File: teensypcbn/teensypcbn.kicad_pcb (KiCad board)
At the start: 2 copper layers, 4 parts, among them J1 CONN_26X2, J2 CONN_26X2, J3 629104190121, U1 Teensy4.1

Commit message: schema
schema voledig klaar
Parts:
- added BT1: Battery, Connector_JST:JST_PH_S2B-PH-SM4-TB_1x02-1MP_P2.00mm_Horizontal, F.Cu at (188.5, 20.3)
- added C1: 0.1, Capacitor_SMD:C_0603_1608Metric_Pad0.99x1.00mm_HandSolder, F.Cu at (171.6, 27.1)
- added C2: 0.1, Capacitor_SMD:C_0603_1608Metric_Pad0.99x1.00mm_HandSolder, F.Cu at (176.0, 27.2)
- added C3: 0.1, Capacitor_SMD:C_0603_1608Metric_Pad0.99x1.00mm_HandSolder, F.Cu at (195.8, 15.9)
- added C4: 0.1, Capacitor_SMD:C_0603_1608Metric_Pad0.99x1.00mm_HandSolder, F.Cu at (180.3, 27.1)
- added C5: 1000pF, Capacitor_SMD:C_0603_1608Metric_Pad0.99x1.00mm_HandSolder, F.Cu at (195.8, 18.5)
- added C6: 1000pF, Capacitor_SMD:C_0603_1608Metric_Pad0.99x1.00mm_HandSolder, F.Cu at (195.8, 21.0)
- added J4: SS-7188S-A-NF, SamacSys_Parts:SS-7188S-A-NF, F.Cu at (192.0, 49.3)
- added R1: R_US, Resistor_SMD:R_0603_1608Metric, F.Cu at (195.6, 23.6)
- added R2: R_US, Resistor_SMD:R_0603_1608Metric, F.Cu at (195.6, 26.1)
- added R3: R_US, Resistor_SMD:R_0603_1608Metric, F.Cu at (184.5, 28.7)
- added R4: R_US, Resistor_SMD:R_0603_1608Metric, F.Cu at (188.4, 27.2)
- added T1: HX1198FNLT, SamacSys_Parts:HX1198FNLT, B.Cu at (191.8, 78.5)
- moved J3 15.2 mm to (157.4, 67.0)
- moved J1 1.77 mm to (107.7, 65.2)
- moved J2 0.58 mm to (214.3, 128.9)
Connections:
- net Net-(U1-Pad61) renamed /LED0
- U1 pad 60: Net-(U1-Pad60) -> /RP
- U1 pad 62: Net-(U1-Pad62) -> /TN
- U1 pad 63: Net-(U1-Pad63) -> /TP
- U1 pad 64: Net-(U1-Pad64) -> GND
- U1 pad 65: Net-(U1-Pad65) -> /RN
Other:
- board outline added: 111.5 x 73.7 mm

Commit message: routing
routing begonnen
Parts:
- BT1: footprint Connector_JST:JST_PH_S2B-PH-SM4-TB_1x02-1MP_P2.00mm_Horizontal -> Connector_JST:JST_PH_B2B-PH-SM4-TB_1x02-1MP_P2.00mm_Vertical
- C1, C2, C3, C4, C5, C6, R1, R2, R3, R4: moved to B.Cu
- J3, T1: moved to F.Cu
- moved J1 166.2 mm to (259.0, 134.0), turned to 180 degrees
- moved J3 106.7 mm to (245.0, 128.0)
- moved C6 101.8 mm to (205.0, 122.4), turned to 180 degrees
- moved R4 99.2 mm to (208.8, 124.2), turned to 180 degrees
- moved R3 97.0 mm to (209.0, 122.5), turned to 180 degrees
- moved C5 96.1 mm to (198.4, 114.6), turned to 180 degrees
- moved R1 91.1 mm to (202.2, 114.4), turned to 180 degrees
- moved J4 89.0 mm to (207.0, 137.0), turned to 0 degrees
- moved R2 86.9 mm to (202.1, 112.8), turned to 180 degrees
- moved C3 83.4 mm to (205.3, 98.8), turned to 90 degrees
- moved C1 82.0 mm to (211.6, 98.6), turned to 90 degrees
- moved C2 79.1 mm to (209.8, 98.7), turned to 270 degrees
- moved C4 75.4 mm to (203.4, 98.9), turned to 270 degrees
- moved U1 69.1 mm to (226.0, 106.8), turned to 90 degrees
- moved BT1 66.2 mm to (226.7, 74.3)
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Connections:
- net /LED0 renamed Net-(U1-Pad61)
- net Net-(J4-Pad1) renamed /T1P
- net Net-(J4-Pad2) renamed /T1N
- net Net-(J4-Pad3) renamed /R1P
- net Net-(J4-Pad6) renamed /R1N
- C5 pad 2: Earth -> GND
- C6 pad 2: Earth -> GND
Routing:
- net /R1N: track 0.00 -> 19.1 mm, vias 0 -> 2
- net Net-(R2-Pad1): track 0.00 -> 13.3 mm, vias 0 -> 1
- net /R1P: track 0.00 -> 11.2 mm
- net Net-(R1-Pad1): track 0.00 -> 9.60 mm, vias 0 -> 1
- net Net-(J4-Pad4): track 0.00 -> 8.93 mm
- net Net-(J4-Pad7): track 0.00 -> 8.71 mm
- net GND: track 0.00 -> 8.50 mm, vias 0 -> 1
- net /T1N: track 0.00 -> 8.11 mm
- net Net-(C3-Pad1): track 0.00 -> 5.14 mm, vias 0 -> 1
- net Net-(C1-Pad1): track 0.00 -> 5.10 mm, vias 0 -> 1
- net Net-(C6-Pad1): track 0.00 -> 4.79 mm
- net Net-(C5-Pad1): track 0.00 -> 1.64 mm
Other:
- board size 111.5 x 73.7 mm -> 71 x 68 mm

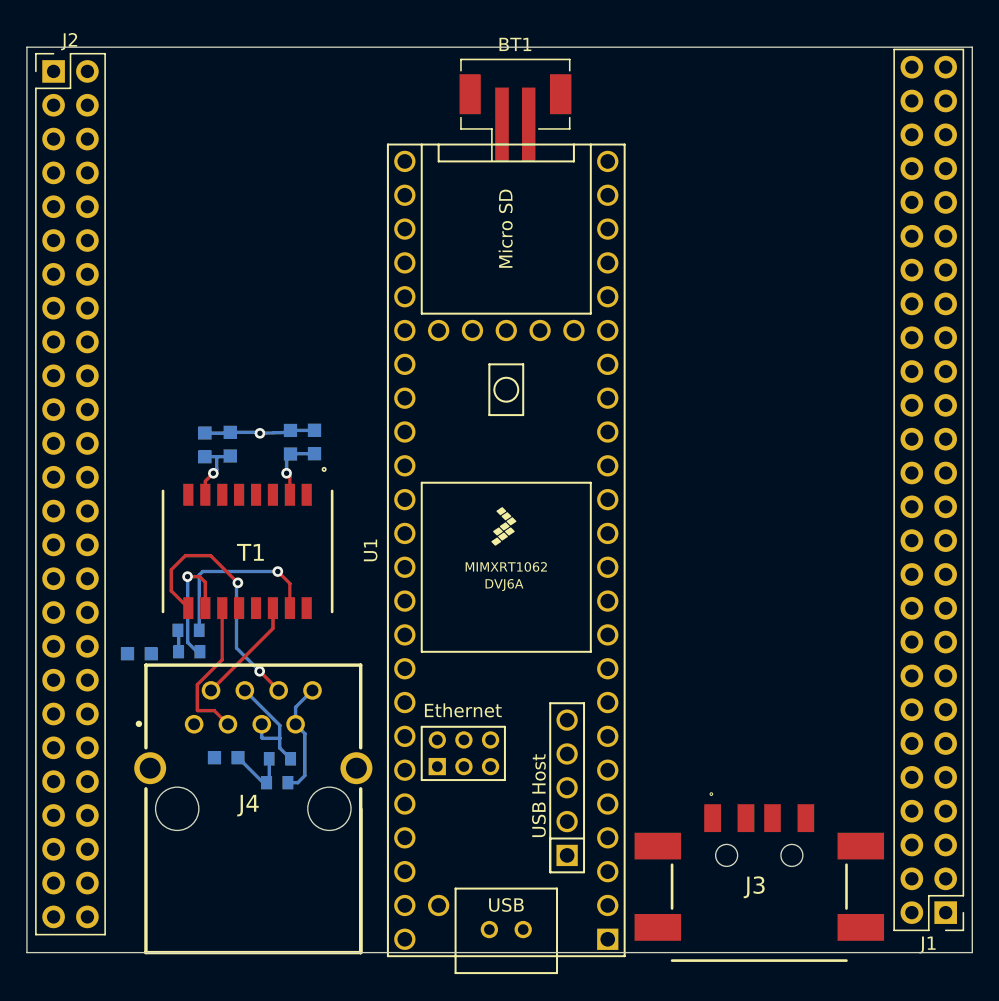
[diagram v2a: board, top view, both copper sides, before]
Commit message: pcb
ethernet en usb nog te routen
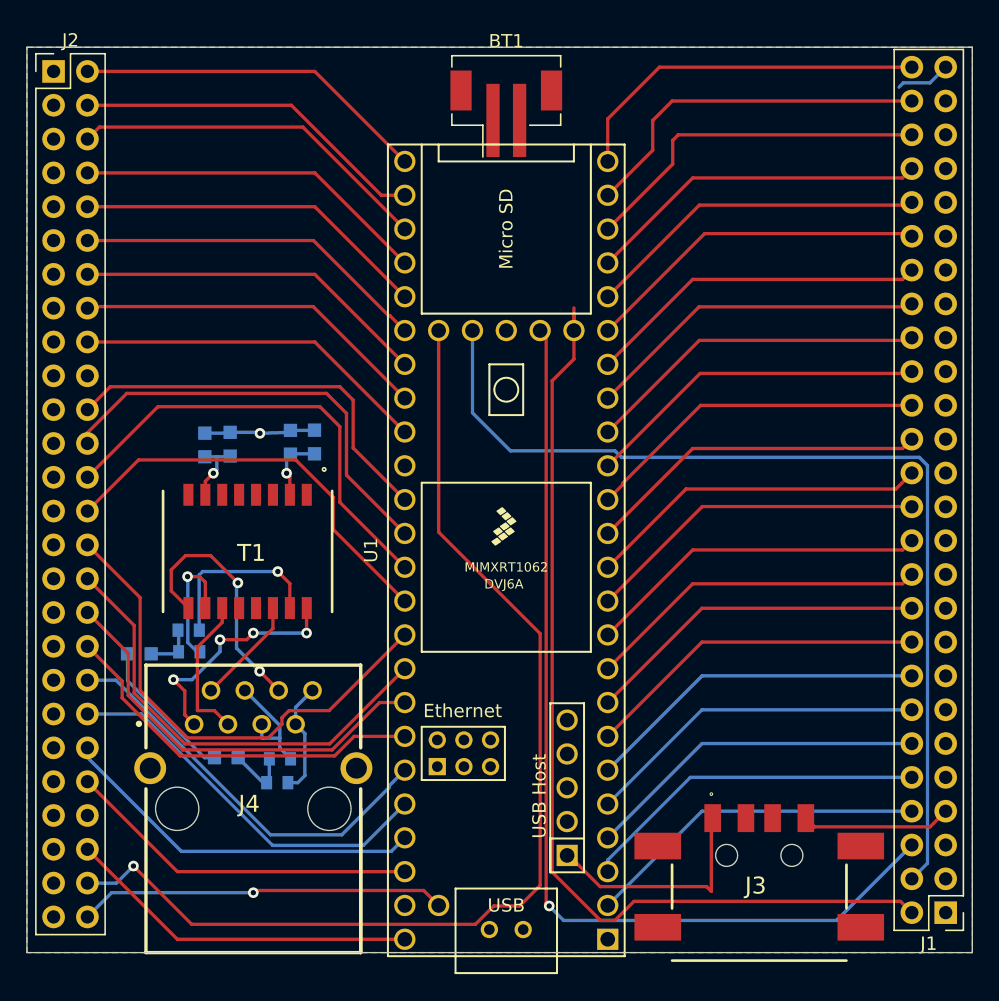
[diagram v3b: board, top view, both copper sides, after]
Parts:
- moved BT1 0.74 mm to (226.0, 74.0)
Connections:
- J2 pad 15: Net-(J2-Pad15) -> GND
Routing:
- net Net-(J2-Pad50): track 0.00 -> 82.4 mm, vias 0 -> 1
- net Net-(BT1-Pad1): track 0.00 -> 73.7 mm
- net Net-(J1-Pad6): track 0.00 -> 73.5 mm, vias 0 -> 1
- net Net-(J1-Pad4): track 0.00 -> 73.5 mm
- net Net-(J2-Pad30): track 0.00 -> 37.4 mm
- net Net-(J2-Pad26): track 0.00 -> 34.4 mm
- net Net-(J2-Pad32): track 0.00 -> 34.3 mm
- net Net-(J2-Pad24): track 0.00 -> 32.9 mm
- net Net-(J2-Pad34): track 0.00 -> 31.4 mm
- net Net-(J2-Pad28): track 0.00 -> 31.2 mm
- net Net-(J2-Pad38): track 0.00 -> 30.7 mm
- net Net-(J2-Pad22): track 0.00 -> 30.2 mm
- net Net-(J2-Pad40): track 0.00 -> 29.2 mm
- net Net-(J2-Pad36): track 0.00 -> 28.6 mm
- net Net-(J2-Pad42): track 0.00 -> 27.9 mm
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- added copper zone on B.Cu, net GND

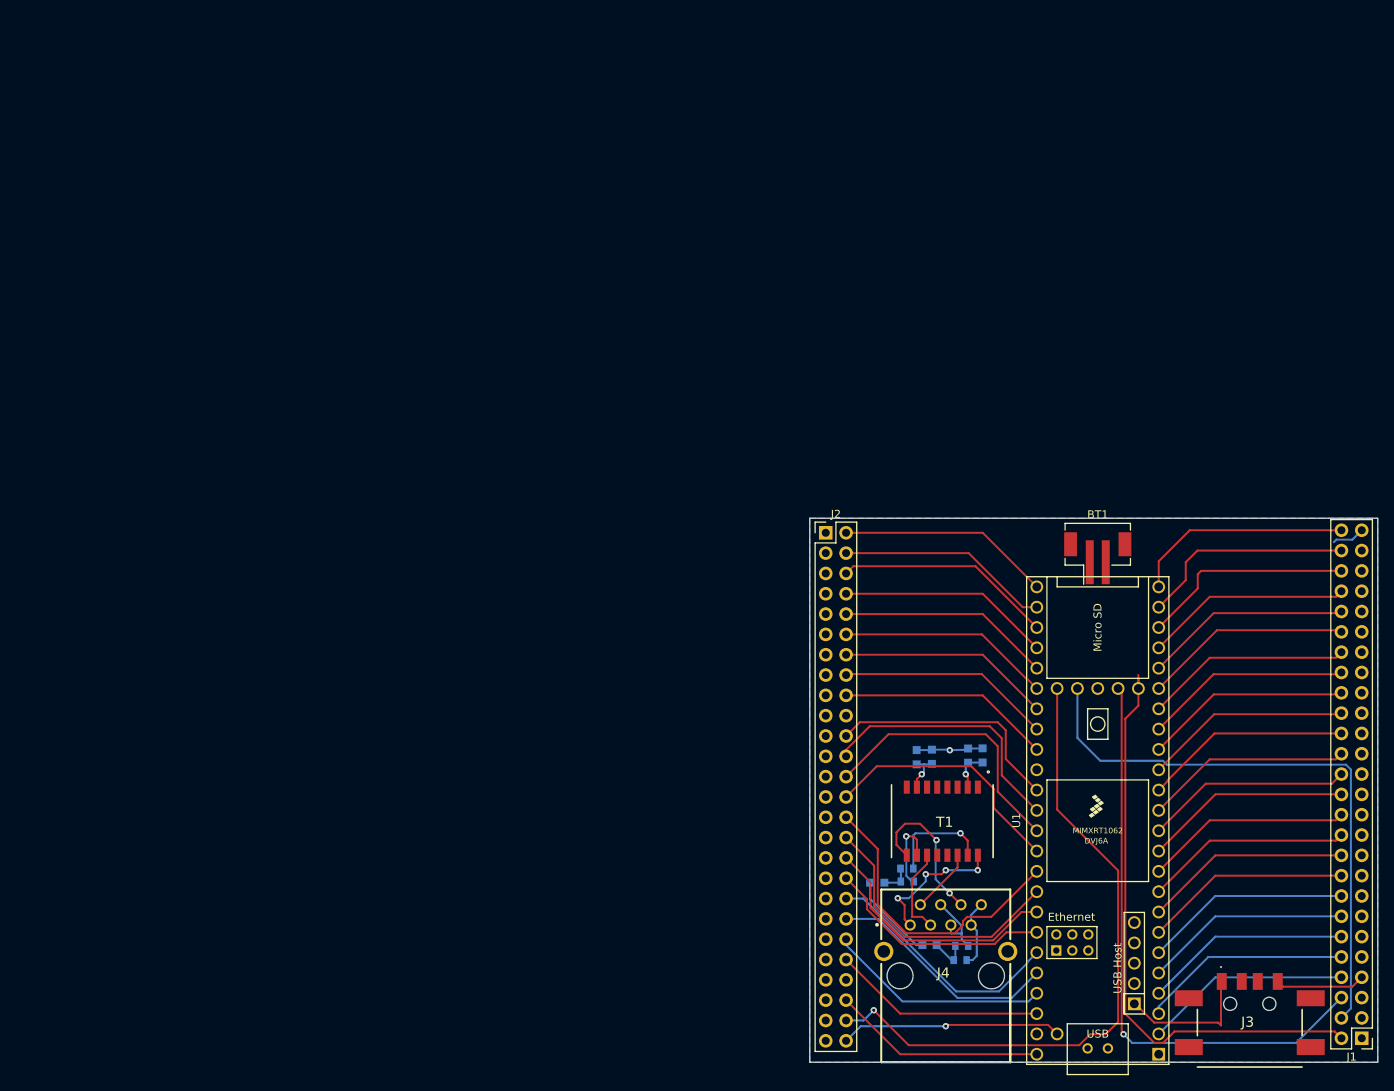
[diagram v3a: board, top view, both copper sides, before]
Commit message: routing V2
routing gestart met de juiste connector
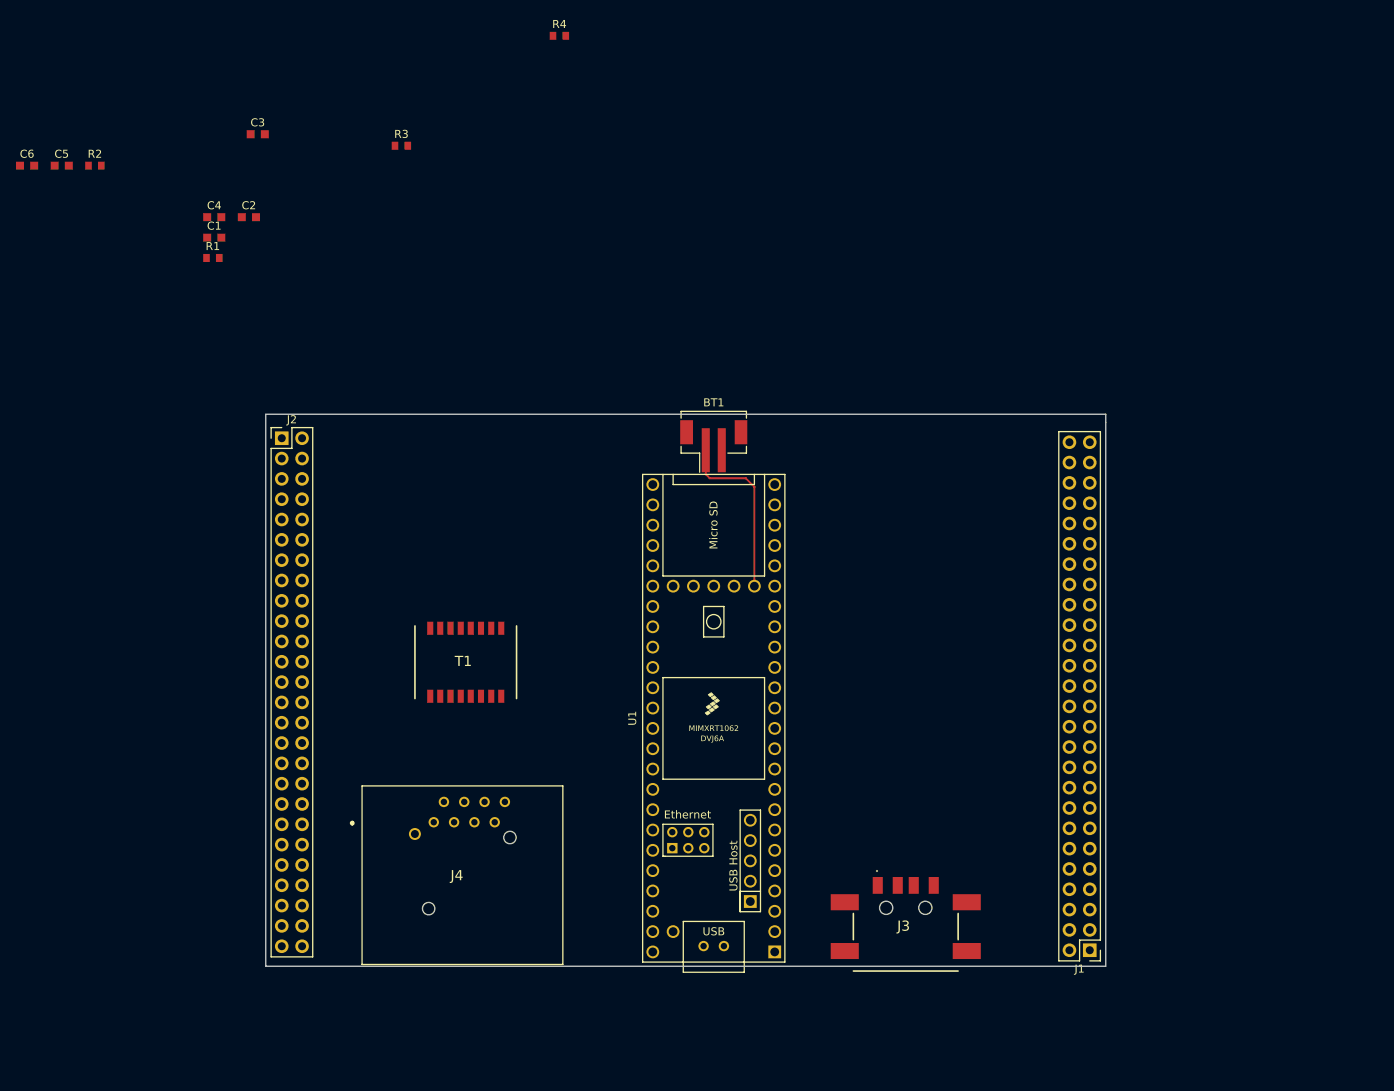
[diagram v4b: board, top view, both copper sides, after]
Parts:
- C1, C2, C3, C4, C5, C6, R1, R2, R3, R4: moved to F.Cu
- J4: value SS-7188S-A-NF -> NE8FAH-C5; footprint SamacSys_Parts:SS-7188S-A-NF -> SamacSys_Parts:NE8FAHC5
- moved C6 149.1 mm to (92.2, 24.9), turned to 0 degrees
- moved C5 135.7 mm to (96.5, 24.9), turned to 0 degrees
- moved R2 134.2 mm to (100.6, 24.9), turned to 0 degrees
- moved R4 125.9 mm to (158.7, 8.71), turned to 0 degrees
- moved R3 122.1 mm to (139.0, 22.4), turned to 0 degrees
- moved R1 116.7 mm to (115.4, 36.5), turned to 0 degrees
- moved C1 115.8 mm to (115.6, 33.9), turned to 0 degrees
- moved C3 114.7 mm to (121.0, 21.0), turned to 0 degrees
- moved C2 112.3 mm to (119.9, 31.4), turned to 0 degrees
- moved C4 110.8 mm to (115.6, 31.4), turned to 0 degrees
- moved J4 70.7 mm to (143.0, 107.0), turned to 180 degrees
- moved J2 69.0 mm to (124.0, 59.0)
- moved T1 62.8 mm to (147.0, 87.0), turned to 0 degrees
- moved BT1 50.0 mm to (178.0, 60.0)
- moved U1 49.7 mm to (178.0, 94.0)
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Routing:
- net Net-(J2-Pad50): track 82.4 -> 0.00 mm, vias 1 -> 0
- net Net-(J1-Pad6): track 73.5 -> 0.00 mm, vias 1 -> 0
- net Net-(J1-Pad4): track 73.5 -> 0.00 mm
- net Net-(BT1-Pad1): track 73.7 -> 22.1 mm
- net Net-(J2-Pad30): track 37.4 -> 0.00 mm
- net GND: track 34.9 -> 0.00 mm, vias 1 -> 0
- net Net-(J2-Pad26): track 34.4 -> 0.00 mm
- net Net-(J2-Pad32): track 34.3 -> 0.00 mm
- net Net-(J2-Pad24): track 32.9 -> 0.00 mm
- net Net-(J2-Pad34): track 31.4 -> 0.00 mm
- net Net-(J2-Pad28): track 31.2 -> 0.00 mm
- net Net-(J2-Pad38): track 30.7 -> 0.00 mm
- net Net-(J2-Pad22): track 30.2 -> 0.00 mm
- net Net-(J2-Pad40): track 29.2 -> 0.00 mm
- net Net-(J2-Pad36): track 28.6 -> 0.00 mm
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- removed copper zone on B.Cu, net GND
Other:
- board size 71 x 68 mm -> 105 x 69 mm

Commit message: placment
placment bijna klaar
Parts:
- moved T1 7.62 mm to (150.0, 94.0)
- moved J4 3.00 mm to (146.0, 107.0)
- moved J3 2.00 mm to (204.0, 116.0)

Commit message: bijna klaar
bijna klaar met routen
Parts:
- C1, C2, C3, C4, C5, C6, R1, R2, R3, R4: moved to B.Cu
- moved C6 107.0 mm to (162.0, 106.0)
- moved R4 96.3 mm to (158.5, 105.0)
- moved R3 86.3 mm to (158.5, 106.5)
- moved C5 85.9 mm to (144.4, 96.2), turned to 180 degrees
- moved R2 84.1 mm to (148.1, 94.3), turned to 180 degrees
- moved C3 76.2 mm to (141.8, 94.3), turned to 180 degrees
- moved R1 68.1 mm to (148.3, 96.1), turned to 180 degrees
- moved C4 66.7 mm to (142.1, 92.6)
- moved C2 64.1 mm to (151.4, 87.2)
- moved C1 62.7 mm to (151.3, 85.5), turned to 180 degrees
- moved T1 0.50 mm to (149.5, 94.0), turned to 180 degrees
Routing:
- net Net-(J2-Pad50): track 0.00 -> 95.7 mm
- net Net-(J1-Pad6): track 0.00 -> 87.4 mm
- net Net-(J1-Pad4): track 0.00 -> 84.9 mm, vias 0 -> 1
- net Net-(BT1-Pad1): track 22.1 -> 102.8 mm, vias 0 -> 2
- net GND: track 0.00 -> 62.8 mm, vias 0 -> 7
- net Net-(J2-Pad28): track 0.00 -> 48.7 mm, vias 0 -> 1
- net Net-(J2-Pad22): track 0.00 -> 48.6 mm
- net Net-(J2-Pad40): track 0.00 -> 47.6 mm
- net Net-(J2-Pad4): track 0.00 -> 47.3 mm
- net Net-(J2-Pad52): track 0.00 -> 47.1 mm
- net Net-(J2-Pad26): track 0.00 -> 46.3 mm
- net Net-(J2-Pad6): track 0.00 -> 46.2 mm
- net Net-(J2-Pad42): track 0.00 -> 46.2 mm
- net Net-(J2-Pad38): track 0.00 -> 46.2 mm
- net Net-(J2-Pad24): track 0.00 -> 46.2 mm
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- added copper zone on B.Cu, net GND
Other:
- net class Default: trace_width 0.25 -> 0.2

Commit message: routing klaar
routing klaar , bom moet nog aangepast worden
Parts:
- C1, C2, C3, C4: value 0.1 -> 0.1uF
- R1, R2, R3, R4: value R_US -> 75ohm
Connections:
- J1 pad 15: Net-(J1-Pad15) -> GND
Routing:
- net Net-(J2-Pad30): track 0.00 -> 54.8 mm
- net Net-(J2-Pad32): track 0.00 -> 53.4 mm
- net Net-(J2-Pad34): track 0.00 -> 52.0 mm
- net Net-(J2-Pad36): track 2.73 -> 51.1 mm, vias 1 -> 0
- net GND: track 62.8 -> 103.4 mm, vias 7 -> 11
- net (no net): track 0.00 -> 16.2 mm, vias 0 -> 2
- net /RN: track 38.6 -> 42.5 mm
- net Net-(J2-Pad38): track 46.2 -> 48.9 mm
- net /TP: track 44.5 -> 42.7 mm
- net Net-(J2-Pad28): track 48.7 -> 47.7 mm

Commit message: fab files
fabrication files toegevoegd
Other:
- board text added: "Rev 1 8/15/2020"
- board text added: "Teensy Dev board Ontworpen door BDL"
